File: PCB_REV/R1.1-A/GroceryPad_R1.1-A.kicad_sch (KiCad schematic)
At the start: 7 parts, among them SW1 SW_SPST, U1 ESP32-C3_SUPERMINI_TH

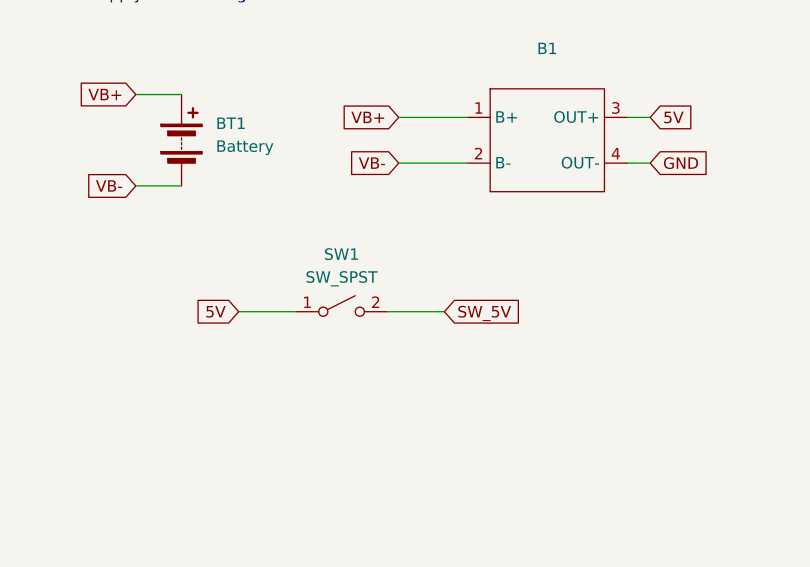
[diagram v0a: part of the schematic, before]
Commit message: Power switch and case update
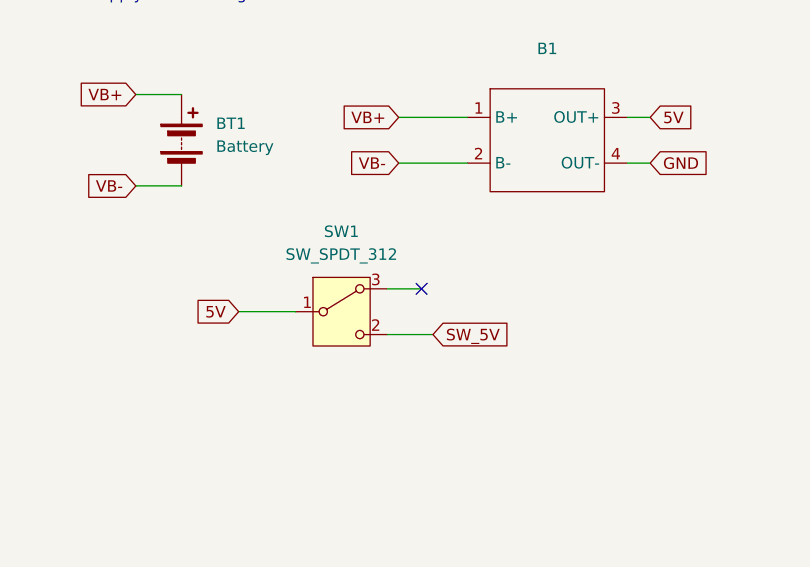
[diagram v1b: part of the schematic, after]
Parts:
- removed SW1: SW_SPST, Switch:SPST Switch, symbol My_Switch:SW_SPST
- added SW1: SW_SPDT_312, Switch:SPDT Slide Switch, symbol Switch:SW_SPDT_312
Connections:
- net 5V: now also SW1.1 (B)
- net SW_5V: now also SW1.2 (C)
- no-connect marks 6 -> 7
